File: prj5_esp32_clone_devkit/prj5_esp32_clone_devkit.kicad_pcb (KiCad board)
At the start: 4 copper layers, 30.7 x 57.2 mm, 36 parts, among them J1 USB_B_Micro, J2 Conn_01x19_Pin, J3 Conn_01x19_Pin, Q1 MMSS8050-H-TP, Q2 MMSS8050-H-TP, SW1 SW_Push, SW2 SW_Push, U1 CP2102N-A01-GQFN28, U2 AMS1117-3.3

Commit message: Aggiunte informazioni sul PCB
Docs: aggiunte board characteristics
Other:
- board text added: "0,1000 mm / 0,0000 mm"
- board text added: "0,3000 mm"
- board text added: "1,6000 mm"
- board text added: "30,6832 mm x 57,1500 mm"
- board text added: "BOARD CHARACTERISTICS"
- board text added: "Board Thickness:"
- board text added: "Board overall dimensions:"
- board text added: "Castellated pads:"
- board text added: "Copper Finish:"
- board text added: "Copper Layer Count:"
- board text added: "Edge card connectors:"
- board text added: "Impedance Control:"
- board text added: "Min hole diameter:"
- board text added: "Min track/spacing:"
- board text added: "No"
- board text added: "None"
- board text added: "Plated Board Edge:"
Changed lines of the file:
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@@
       (plot_on_all_layers_selection 0x0000000_00000000)
       (disableapertmacros false)
-      (usegerberextensions false)
+      (usegerberextensions true)
       (usegerberattributes true)
       (usegerberadvancedattributes true)
@@
       (outputformat 1)
       (mirror false)
-      (drillshape 1)
+      (drillshape 0)
       (scaleselection 1)
-      (outputdirectory "")
+      (outputdirectory "ESP32-Devkit-Clione-Gerbers/")
     )
   )
@@
     (fp_line (start 2.5 2.5) (end 2.5 -2.5)
       (stroke (width 0.1) (type solid)) (layer "B.Fab"))
-    (pad "" smd roundrect locked (at -0.675 -0.675 180) (size 1.09 1.09) (layers "B.Paste") (roundrect_rratio 0.229358))
-    (pad "" smd roundrect locked (at -0.675 0.675 180) (size 1.09 1.09) (layers "B.Paste") (roundrect_rratio 0.229358))
-    (pad "" smd roundrect locked (at 0.675 -0.675 180) (size 1.09 1.09) (layers "B.Paste") (roundrect_rratio 0.229358))
-    (pad "" smd roundrect locked (at 0.675 0.675 180) (size 1.09 1.09) (layers "B.Paste") (roundrect_rratio 0.229358))
+    (pad "" smd roundrect locked (at -0.675 -0.675 180) (size 1.09 1.09) (layers "B.Paste") (roundrect_rratio 0.2293577982))
+    (pad "" smd roundrect locked (at -0.675 0.675 180) (size 1.09 1.09) (layers "B.Paste") (roundrect_rratio 0.2293577982))
+    (pad "" smd roundrect locked (at 0.675 -0.675 180) (size 1.09 1.09) (layers "B.Paste") (roundrect_rratio 0.2293577982))
+    (pad "" smd roundrect locked (at 0.675 0.675 180) (size 1.09 1.09) (layers "B.Paste") (roundrect_rratio 0.2293577982))
     (pad "1" smd roundrect locked (at -2.3625 1.5 180) (size 0.975 0.25) (layers "B.Cu" "B.Paste" "B.Mask") (roundrect_rratio 0.25)
       (net 52 "unconnected-(U1-DCD-Pad1)") (pinfunction "DCD") (pintype "input+no_connect"))
@@
     (effects (font (size 0.8 0.8) (thickness 0.1)) (justify left bottom))
   )
+  (gr_text "No" (at 115.011538 109.4092) (layer "User.1")
+    (effects (font (size 1.5 1.5) (thickness 0.2)) (justify left top))
+  )
+  (gr_text "No" (at 55.911543 113.3662) (layer "User.1")
+    (effects (font (size 1.5 1.5) (thickness 0.2)) (justify left top))
+  )
+  (gr_text "BOARD CHARACTERISTICS" (at 22.5044 88.0872) (layer "User.1")
+    (effects (font (size 2 2) (thickness 0.4)) (justify left top))
+  )
+  (gr_text "Plated Board Edge: " (at 90.068681 109.4092) (layer "User.1")
+    (effects (font (size 1.5 1.5) (thickness 0.2)) (justify left top))
+  )
+  (gr_text "Copper Finish: " (at 23.2544 105.4522) (layer "User.1")
+    (effects (font (size 1.5 1.5) (thickness 0.2)) (justify left top))
+  )
+  (gr_text "0,3000 mm" (at 115.011538 101.4952) (layer "User.1")
+    (effects (font (size 1.5 1.5) (thickness 0.2)) (justify left top))
+  )
+  (gr_text "None" (at 55.911543 105.4522) (layer "User.1")
+    (effects (font (size 1.5 1.5) (thickness 0.2)) (justify left top))
+  )
+  (gr_text "Edge card connectors: " (at 23.2544 113.3662) (layer "User.1")
+    (effects (font (size 1.5 1.5) (thickness 0.2)) (justify left top))
+  )
+  (gr_text "Board overall dimensions: " (at 23.2544 97.5382) (layer "User.1")
+    (effects (font (size 1.5 1.5) (thickness 0.2)) (justify left top))
+  )
+  (gr_text "No" (at 115.011538 105.4522) (layer "User.1")
+    (effects (font (size 1.5 1.5) (thickness 0.2)) (justify left top))
+  )
+  (gr_text "Impedance Control: " (at 90.068681 105.4522) (layer "User.1")
+    (effects (font (size 1.5 1.5) (thickness 0.2)) (justify left top))
+  )
+  (gr_text "Min track/spacing: " (at 23.2544 101.4952) (layer "User.1")
+    (effects (font (size 1.5 1.5) (thickness 0.2)) (justify left top))
+  )
+  (gr_text "0,1000 mm / 0,0000 mm" (at 55.911543 101.4952) (layer "User.1")
+    (effects (font (size 1.5 1.5) (thickness 0.2)) (justify left top))
+  )
+  (gr_text "4" (at 55.911543 93.5812) (layer "User.1")
+    (effects (font (size 1.5 1.5) (thickness 0.2)) (justify left top))
+  )
+  (gr_text "No" (at 55.911543 109.4092) (layer "User.1")
+    (effects (font (size 1.5 1.5) (thickness 0.2)) (justify left top))
+  )
+  (gr_text "1,6000 mm" (at 115.011538 93.5812) (layer "User.1")
+    (effects (font (size 1.5 1.5) (thickness 0.2)) (justify left top))
+  )
+  (gr_text "Castellated pads: " (at 23.2544 109.4092) (layer "User.1")
+    (effects (font (size 1.5 1.5) (thickness 0.2)) (justify left top))
+  )
+  (gr_text "30,6832 mm x 57,1500 mm" (at 55.911543 97.5382) (layer "User.1")
+    (effects (font (size 1.5 1.5) (thickness 0.2)) (justify left top))
+  )
+  (gr_text "Copper Layer Count: " (at 23.2544 93.5812) (layer "User.1")
+    (effects (font (size 1.5 1.5) (thickness 0.2)) (justify left top))
+  )
+  (gr_text "Board Thickness: " (at 90.068681 93.5812) (layer "User.1")
+    (effects (font (size 1.5 1.5) (thickness 0.2)) (justify left top))
+  )
+  (gr_text "" (at 115.011538 97.5382) (layer "User.1")
+    (effects (font (size 1.5 1.5) (thickness 0.2)) (justify left top))
+  )
+  (gr_text "" (at 90.068681 97.5382) (layer "User.1")
+    (effects (font (size 1.5 1.5) (thickness 0.2)) (justify left top))
+  )
+  (gr_text "Min hole diameter: " (at 90.068681 101.4952) (layer "User.1")
+    (effects (font (size 1.5 1.5) (thickness 0.2)) (justify left top))
+  )
+  (dimension (type aligned) (layer "User.1")
+    (pts (xy 167.7416 78.74) (xy 137.0584 78.7908))
+    (height 12.005834)
+    (gr_text "30,6832 mm" (at 152.378219 65.609584 0.09486047543) (layer "User.1")
+      (effects (font (size 1 1) (thickness 0.15)))
+    )
+    (format (prefix "") (suffix "") (units 3) (units_format 1) (precision 4))
+    (style (thickness 0.15) (arrow_length 1.27) (text_position_mode 0) (extension_height 0.58642) (extension_offset 0.5) keep_text_aligned)
+  )
+  (dimension (type aligned) (layer "User.1")
+    (pts (xy 152.4 127.7112) (xy 152.4 70.5612))
+    (height 24.2824)
+    (gr_text "57,1500 mm" (at 175.5324 99.1362 90) (layer "User.1")
+      (effects (font (size 1 1) (thickness 0.15)))
+    )
+    (format (prefix "") (suffix "") (units 3) (units_format 1) (precision 4))
+    (style (thickness 0.15) (arrow_length 1.27) (text_position_mode 0) (extension_height 0.58642) (extension_offset 0.5) keep_text_aligned)
+  )
   (segment (start 154.92094 105.50526) (end 155.1432 105.283) (width 0.25) (layer "F.Cu") (net 1))
   (segment (start 154.92094 107.442) (end 154.92094 105.50526) (width 0.25) (layer "F.Cu") (net 1))
@@
     )
   )
+  (group "group-boardCharacteristics" (id b01f1e33-7095-4dd8-af8a-071437f39e6f)
+    (members
+      265bb63c-41ec-4d1e-af5f-984fa0b32016
+      41426d77-1c07-4276-bcaf-3c00d4793a78
+      4316c30b-74dd-43d9-b3e3-4ffbed632f28
+      4528d556-fd85-4efa-98c3-627a0f21961a
+      5d76c84b-ec56-4b25-801d-67e4c29c2254
+      635c88ff-41d1-4ada-bc5a-4b19a14d09e3
+      664bd7fb-b871-4bd1-a8ec-418f3cfed0d3
+      6f3e7fde-7f3d-4857-8f80-a3a966cfedb6
+      6f798625-9850-49c7-8166-3d830efd7289
+      81710d79-865c-4ff3-8225-de7f2776c4fb
+      86f27f5a-d18d-42a3-ab45-1232d5740550
+      9669098a-2076-4d55-8321-4ac336a78cd6
+      a14fc2a4-f483-4c15-a1b4-41c595f062b0
+      a1e932c0-a13f-49cd-aee6-f321bc1538ab
+      ad17c200-e8d4-485f-a157-a43369be68bd
+      ca089581-cc7e-42d0-9da9-cc14fb3d59c8
+      cb3cd3dd-6c81-4ebd-bb4f-b2956a847da3
+      e27701c2-84ce-45b4-a522-484e1070b004
+      e8dc80ce-ca81-40bf-b0a1-7d54728b8b95
+      eb166e9d-2be2-4bc0-99a6-dcda4c485c29
+      eb236028-c8a3-41c3-b00d-37bf4dedfa09
+      ed2a73b2-9df5-4498-be76-b118becb86e6
+      fc1e2e4e-ce45-4e04-bf44-f53a07368d37
+    )
+  )

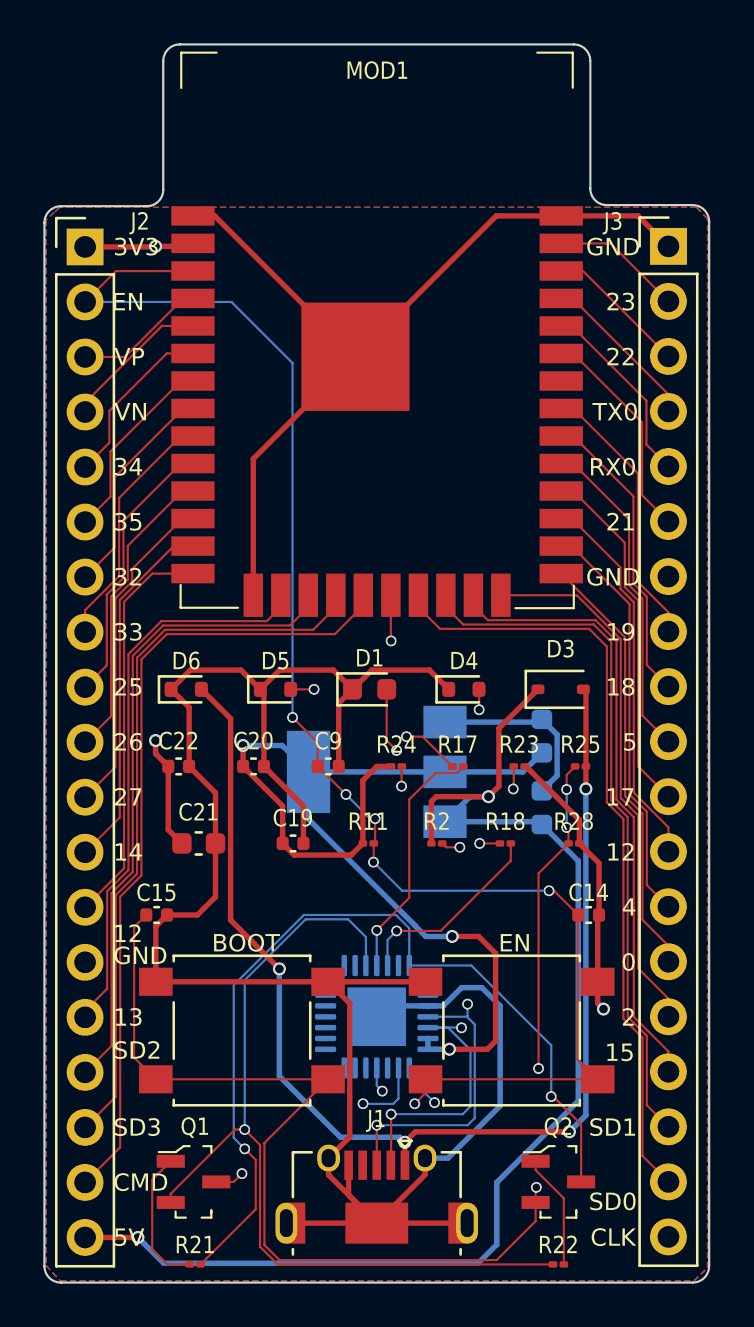
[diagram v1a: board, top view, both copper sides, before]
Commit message: Correzione orientamento Q2
Fix: corretto l'orientamento di Q2 nello schematico
Fix: riportata la correzione sul PCB
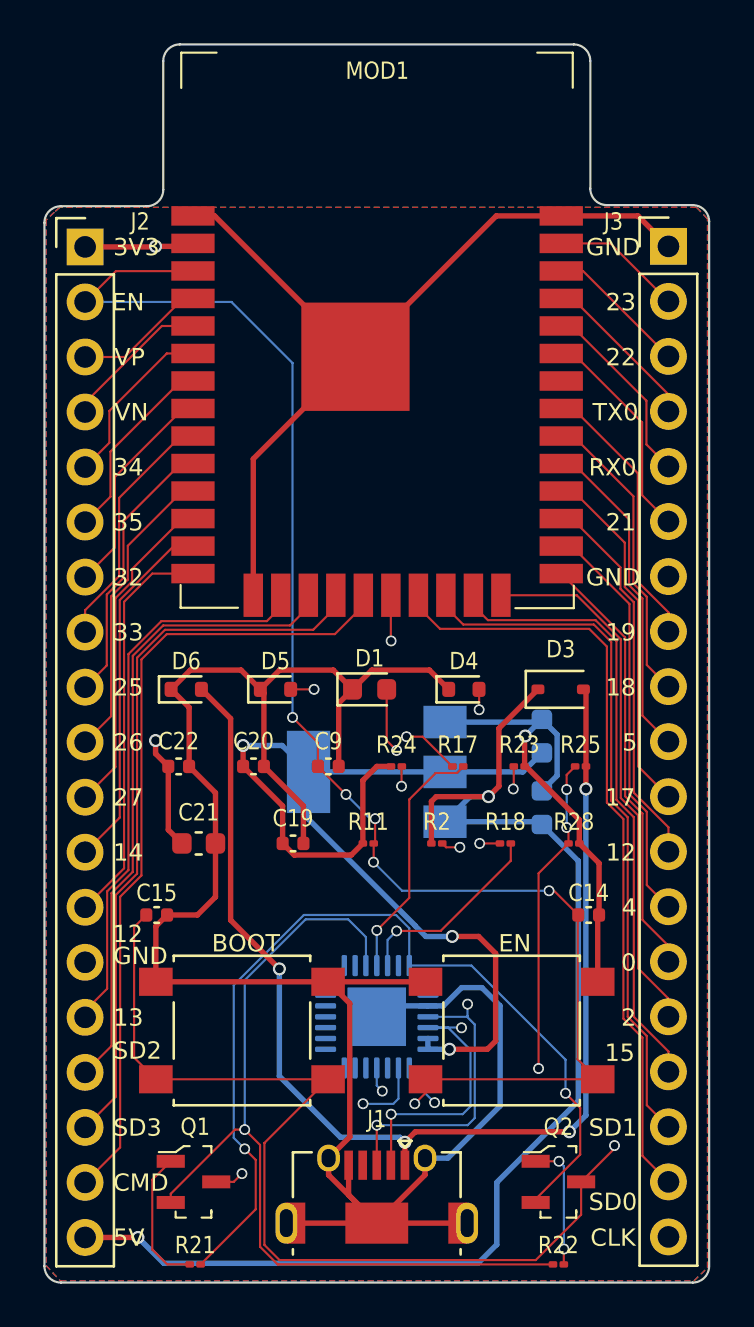
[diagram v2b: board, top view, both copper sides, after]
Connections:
- Q2 pad 2: /IO0 -> /DTR
- Q2 pad 3: /DTR -> /IO0
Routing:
- net /DTR: track 40.8 -> 42.5 mm
- net GND: track 160.8 -> 161.9 mm
- net /IO0: track 73.1 -> 74.1 mm
- net Net-(Q2-B): track 5.30 -> 5.93 mm, vias 0 -> 2
